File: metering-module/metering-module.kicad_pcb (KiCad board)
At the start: 2 copper layers, 86 x 31 mm, 39 parts, among them J1 North, J2 South, J3 West, J4 East, Q1 MMBT3904, Q2 MMBT3904, U1 LTV-817S, U2 LTV-817S, U3 BA033CC0FP-E2, U4 MAX3486, U5 MAX3486, U6 MCP23009-E_SS

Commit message: Migrate Ethernet, SoC, Metering Modules to KiCad6
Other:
- net class Default removed

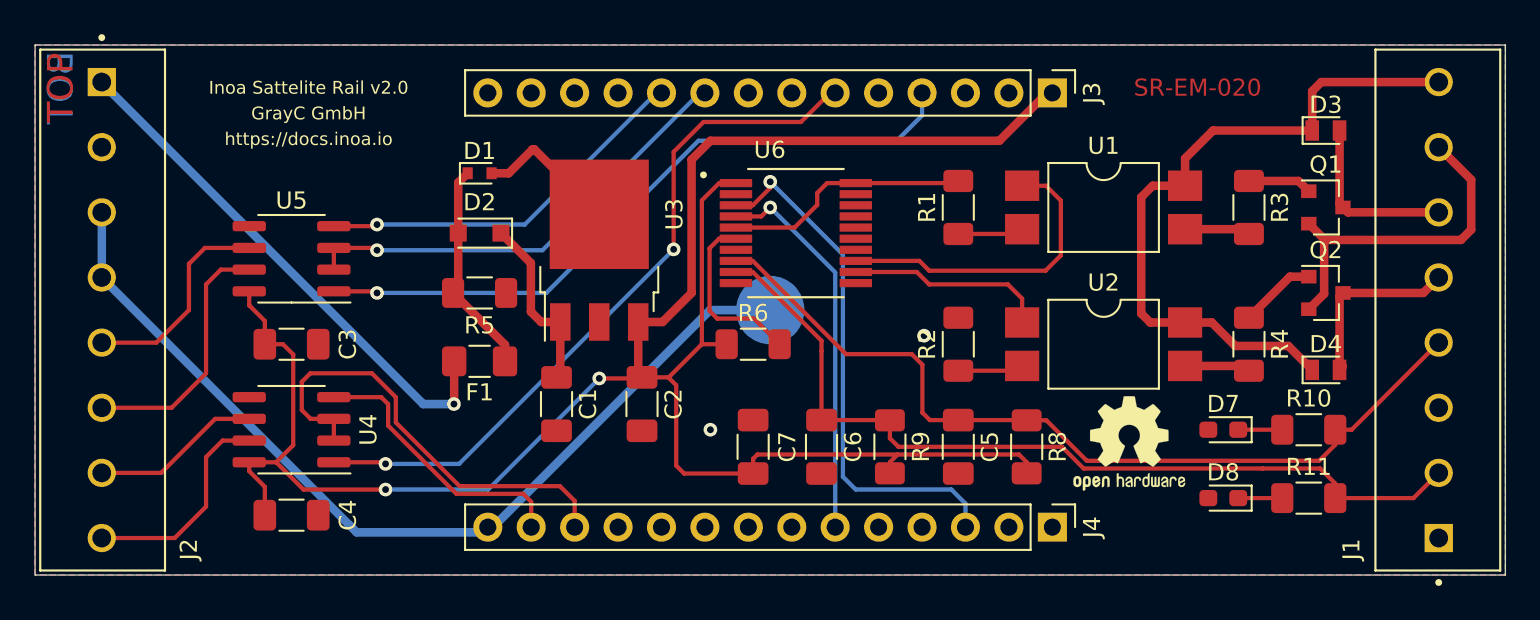
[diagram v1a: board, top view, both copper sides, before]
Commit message: Trim further warnings and errors
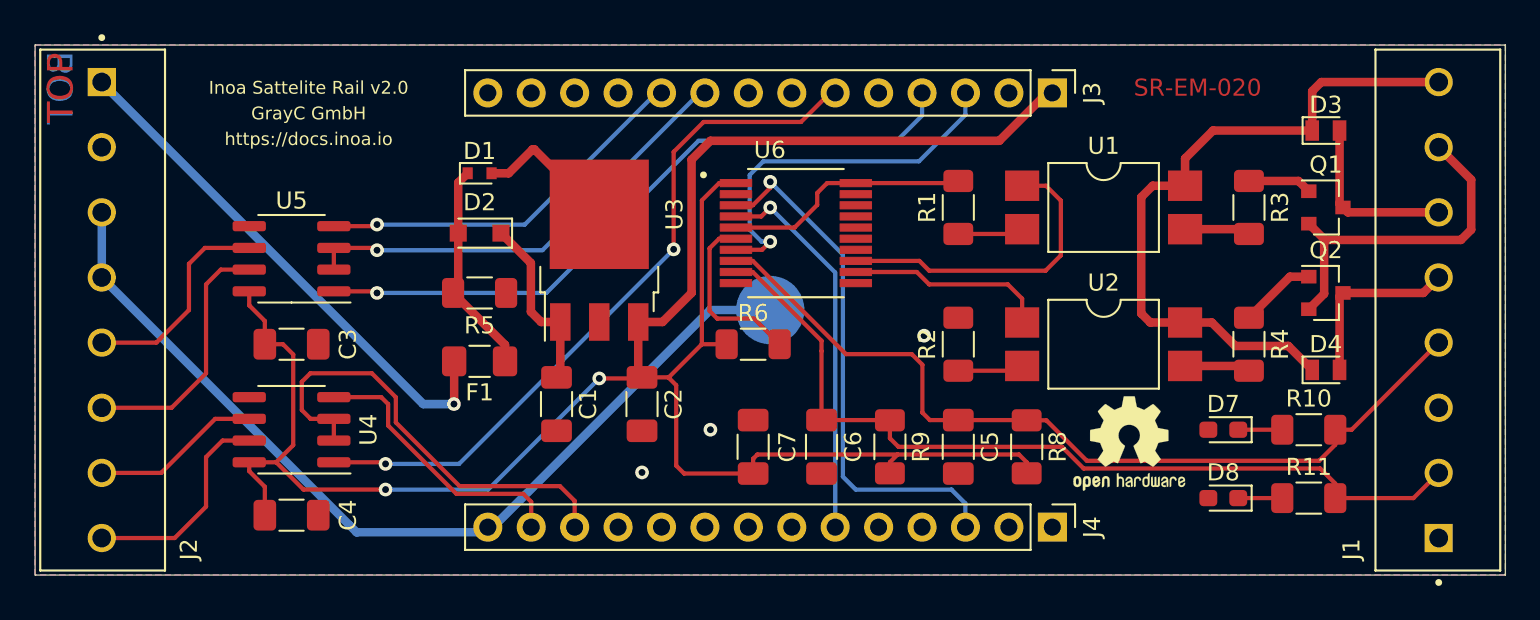
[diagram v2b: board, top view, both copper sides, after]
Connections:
- J3 pad 11: (no net) -> unconnected-(J3-Pad11)
- J3 pad 12: (no net) -> unconnected-(J3-Pad12)
- J3 pad 13: (no net) -> unconnected-(J3-Pad13)
- J3 pad 14: (no net) -> unconnected-(J3-Pad14)
- J3 pad 2: (no net) -> unconnected-(J3-Pad2)
- J3 pad 3: (no net) -> S0_INT
- J3 pad 5: (no net) -> unconnected-(J3-Pad5)
- J3 pad 7: (no net) -> unconnected-(J3-Pad7)
- J3 pad 8: (no net) -> unconnected-(J3-Pad8)
- J4 pad 10: (no net) -> unconnected-(J4-Pad10)
- J4 pad 11: (no net) -> unconnected-(J4-Pad11)
- J4 pad 2: (no net) -> unconnected-(J4-Pad2)
- J4 pad 4: (no net) -> unconnected-(J4-Pad4)
- J4 pad 5: (no net) -> unconnected-(J4-Pad5)
- J4 pad 7: (no net) -> unconnected-(J4-Pad7)
- J4 pad 8: (no net) -> unconnected-(J4-Pad8)
- J4 pad 9: (no net) -> unconnected-(J4-Pad9)
- U6 pad 14: (no net) -> unconnected-(U6-Pad14)
- U6 pad 15: (no net) -> unconnected-(U6-Pad15)
- U6 pad 16: (no net) -> unconnected-(U6-Pad16)
- U6 pad 17: (no net) -> unconnected-(U6-Pad17)
- U6 pad 7: (no net) -> S0_INT
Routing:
- net S0_INT: track 0.00 -> 22.2 mm, vias 0 -> 1
- net GND: vias 2 -> 3
